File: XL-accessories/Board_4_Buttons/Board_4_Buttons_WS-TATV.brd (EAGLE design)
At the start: 156 x 47.9 mm, 1 part

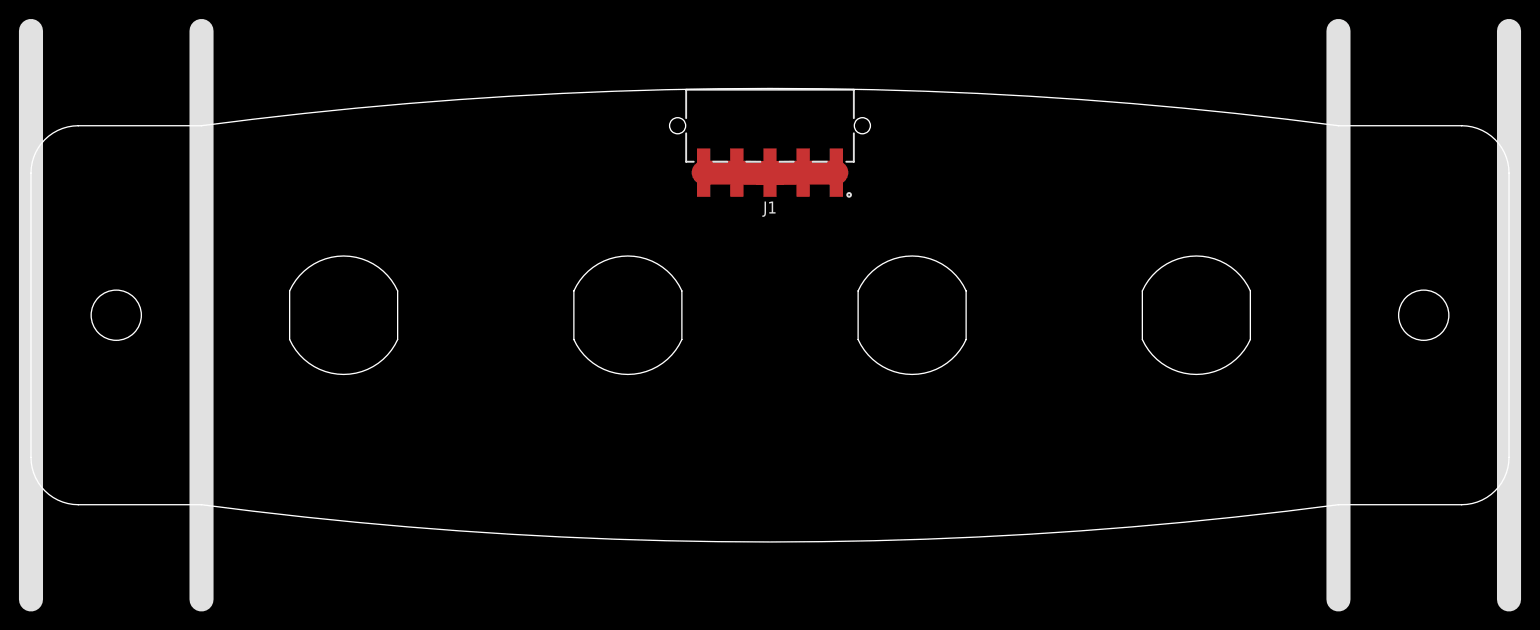
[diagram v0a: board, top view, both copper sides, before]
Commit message: Update grid settings and layer visibility, modify library descriptions, and adjust package details.
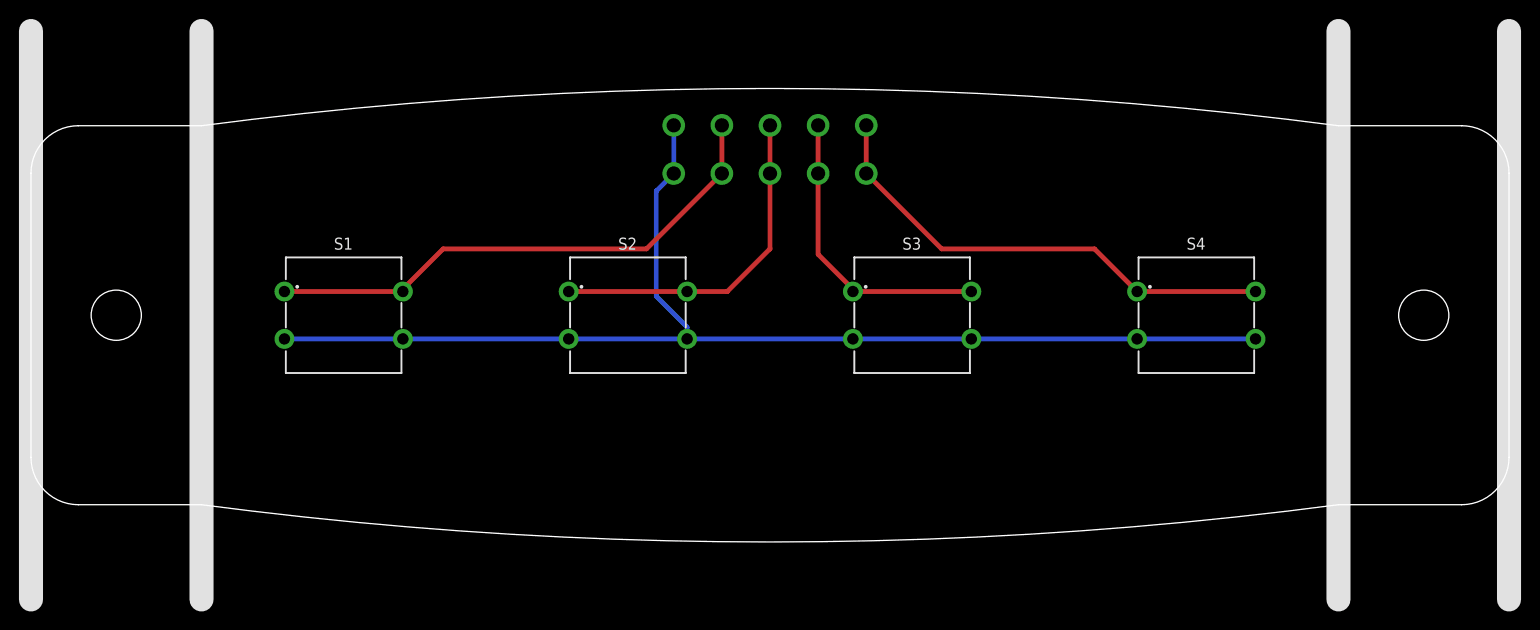
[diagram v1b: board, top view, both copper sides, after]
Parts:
- added S1, S2, S3, S4: (no value), Wurth_Switch_WS-TATV:4304X60737X6
- J1: value (none) -> 638207122005; device Wurth_Connectors_WR-TBL Rising Cage Clamp:691508110305 -> Wurth_Connectors_WR-FAST:638207122005
- moved J1 2.50 mm to (0.00, 17.5), flipped to the bottom
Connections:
- new net N$5: J1.2, J1.A2, S1.1, S1.2
- new net N$6: J1.3, J1.A3, S2.1, S2.2
- new net N$7: J1.4, J1.A4, S3.1, S3.2
- new net N$8: J1.5, J1.A5, S4.1, S4.2
- net N$1: now also J1.A1, S1.3, S1.4, S2.3, S2.4, S3.3, S3.4, S4.3, S4.4; no longer J1.2, J1.3, J1.4, J1.5
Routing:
- net N$1: track 14.1 -> 127.1 mm
- net N$5: track 0.00 -> 56.7 mm
- net N$8: track 0.00 -> 51.3 mm
- net N$6: track 0.00 -> 36.2 mm
- net N$7: track 0.00 -> 31.7 mm
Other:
- outline, holes or cut-outs redrawn
